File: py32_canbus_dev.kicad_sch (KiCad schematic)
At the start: 42 parts, among them J2 Conn_01x18, J3 Conn_01x18, J4 CAN1, J5 USB_B_Micro, SW2 Reset, U1 uA7805, U2 PY32F030K1xT, U3 MCP2518FD-E/QBB, U4 MCP2562FD-E/MF, U5 FT230XQ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

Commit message: Completed schematic and pcb check
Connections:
- net GND: no longer J2.8 (Pin_8), J2.9 (Pin_9)
- net PA11: now also J2.15 (Pin_15); no longer J2.17 (Pin_17)
- net PA12: now also J2.14 (Pin_14); no longer J2.16 (Pin_16)
- net PA15: now also J2.13 (Pin_13); no longer J2.15 (Pin_15)
- net PB3: now also J2.12 (Pin_12); no longer J2.14 (Pin_14)
- net PB4: now also J2.11 (Pin_11); no longer J2.13 (Pin_13)
- net PB5: now also J2.10 (Pin_10); no longer J2.12 (Pin_12)
- net USB_RX: now also J2.8 (Pin_8); no longer J2.10 (Pin_10)
- net USB_TX: now also J2.9 (Pin_9); no longer J2.11 (Pin_11)
- net OSC32IN renamed PA10
- net PA10: now also J2.16 (Pin_16)
- net OSC32OUT renamed PA9
- net PA9: now also J2.17 (Pin_17)
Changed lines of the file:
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@@
 	)
 	(junction
-		(at 232.41 44.45)
-		(diameter 0)
-		(color 0 0 0 0)
-	)
-	(junction
 		(at 130.81 34.29)
 		(diameter 0)
@@
 	)
 	(junction
-		(at 232.41 46.99)
-		(diameter 0)
-		(color 0 0 0 0)
-	)
-	(junction
 		(at 238.76 147.32)
 		(diameter 0)
@@
 	(wire
 		(pts
-			(xy 232.41 46.99) (xy 232.41 82.55)
-		)
-		(stroke
-			(width 0)
-			(type default)
-		)
-	)
-	(wire
-		(pts
 			(xy 52.07 135.89) (xy 52.07 139.7)
 		)
@@
 	(wire
 		(pts
-			(xy 232.41 41.91) (xy 232.41 44.45)
+			(xy 232.41 41.91) (xy 232.41 82.55)
 		)
 		(stroke
@@
 	(wire
 		(pts
-			(xy 232.41 46.99) (xy 245.11 46.99)
-		)
-		(stroke
-			(width 0)
-			(type default)
-		)
-	)
-	(wire
-		(pts
 			(xy 139.7 175.26) (xy 139.7 177.8)
 		)
@@
 	(wire
 		(pts
-			(xy 232.41 44.45) (xy 232.41 46.99)
-		)
-		(stroke
-			(width 0)
-			(type default)
-		)
-	)
-	(wire
-		(pts
-			(xy 232.41 44.45) (xy 245.11 44.45)
-		)
-		(stroke
-			(width 0)
-			(type default)
-		)
-	)
-	(wire
-		(pts
 			(xy 27.94 59.69) (xy 27.94 49.53)
 		)
@@
 	(global_label "PA15"
 		(shape bidirectional)
-		(at 245.11 62.23 180)
+		(at 245.11 57.15 180)
+		(fields_autoplaced yes)
+		(effects
+			(font
+				(size 1.27 1.27)
+			)
+			(justify right)
+		)
+		(property "Intersheetrefs" "${INTERSHEET_REFS}"
+			(at 237.9193 57.2294 0)
+			(effects
+				(font
+					(size 1.27 1.27)
+				)
+				(justify right)
+				(hide yes)
+			)
+		)
+	)
+	(global_label "PA10"
+		(shape bidirectional)
+		(at 245.11 64.77 180)
 		(fields_autoplaced yes)
 		(effects
@@
 		)
 		(property "Intersheetrefs" "${INTERSHEET_REFS}"
-			(at 237.9193 62.3094 0)
+			(at 236.2359 64.77 0)
 			(effects
 				(font
@@
 		)
 	)
-	(global_label "OSC32OUT"
-		(shape output)
+	(global_label "PA9"
+		(shape bidirectional)
 		(at 162.56 105.41 0)
 		(fields_autoplaced yes)
@@
 		)
 		(property "Intersheetrefs" "${INTERSHEET_REFS}"
-			(at 174.8307 105.4894 0)
+			(at 170.2246 105.41 0)
 			(effects
 				(font
@@
 		)
 	)
-	(global_label "OSC32IN"
-		(shape input)
+	(global_label "PA10"
+		(shape bidirectional)
 		(at 162.56 102.87 0)
 		(fields_autoplaced yes)
@@
 		)
 		(property "Intersheetrefs" "${INTERSHEET_REFS}"
-			(at 173.1374 102.9494 0)
+			(at 171.4341 102.87 0)
 			(effects
 				(font
@@
 		)
 	)
+	(global_label "PA9"
+		(shape bidirectional)
+		(at 245.11 67.31 180)
+		(fields_autoplaced yes)
+		(effects
+			(font
+				(size 1.27 1.27)
+			)
+			(justify right)
+		)
+		(property "Intersheetrefs" "${INTERSHEET_REFS}"
+			(at 237.4454 67.31 0)
+			(effects
+				(font
+					(size 1.27 1.27)
+				)
+				(justify right)
+				(hide yes)
+			)
+		)
+	)
 	(global_label "SPI1-NSS"
 		(shape input)
@@
 	(global_label "PB4"
 		(shape bidirectional)
-		(at 245.11 57.15 180)
+		(at 245.11 52.07 180)
 		(fields_autoplaced yes)
 		(effects
@@
 		)
 		(property "Intersheetrefs" "${INTERSHEET_REFS}"
-			(at 238.9474 57.0706 0)
+			(at 238.9474 51.9906 0)
 			(effects
 				(font
@@
 	(global_label "PB3"
 		(shape bidirectional)
-		(at 245.11 59.69 180)
+		(at 245.11 54.61 180)
 		(fields_autoplaced yes)
 		(effects
@@
 		)
 		(property "Intersheetrefs" "${INTERSHEET_REFS}"
-			(at 238.9474 59.6106 0)
+			(at 238.9474 54.5306 0)
 			(effects
 				(font
@@
 	(global_label "USB_RX"
 		(shape input)
-		(at 245.11 49.53 180)
+		(at 245.11 44.45 180)
 		(fields_autoplaced yes)
 		(effects
@@
 		)
 		(property "Intersheetrefs" "${INTERSHEET_REFS}"
-			(at 234.8677 49.53 0)
+			(at 234.8677 44.45 0)
 			(effects
 				(font
@@
 	(global_label "USB_TX"
 		(shape output)
-		(at 245.11 52.07 180)
+		(at 245.11 46.99 180)
 		(fields_autoplaced yes)
 		(effects
@@
 		)
 		(property "Intersheetrefs" "${INTERSHEET_REFS}"
-			(at 235.1701 52.07 0)
+			(at 235.1701 46.99 0)
 			(effects
 				(font
@@
 	(global_label "PB5"
 		(shape bidirectional)
-		(at 245.11 54.61 180)
+		(at 245.11 49.53 180)
 		(fields_autoplaced yes)
 		(effects
@@
 		)
 		(property "Intersheetrefs" "${INTERSHEET_REFS}"
-			(at 238.9474 54.5306 0)
+			(at 238.9474 49.4506 0)
 			(effects
 				(font
@@
 	(global_label "PA12"
 		(shape bidirectional)
-		(at 245.11 64.77 180)
+		(at 245.11 59.69 180)
 		(fields_autoplaced yes)
 		(effects
@@
 		)
 		(property "Intersheetrefs" "${INTERSHEET_REFS}"
-			(at 237.9193 64.6906 0)
+			(at 237.9193 59.6106 0)
 			(effects
 				(font
@@
 	(global_label "PA11"
 		(shape bidirectional)
-		(at 245.11 67.31 180)
+		(at 245.11 62.23 180)
 		(fields_autoplaced yes)
 		(effects
@@
 		)
 		(property "Intersheetrefs" "${INTERSHEET_REFS}"
-			(at 237.9193 67.2306 0)
+			(at 237.9193 62.1506 0)
 			(effects
 				(font
@@
 			(at 238.76 135.89 0)
 			(effects
-				(font
-					(size 1.27 1.27)
-				)
-				(hide yes)
-			)
-		)
-		(property "Field5" ""
-			(at 238.76 135.89 0)
-			(effects

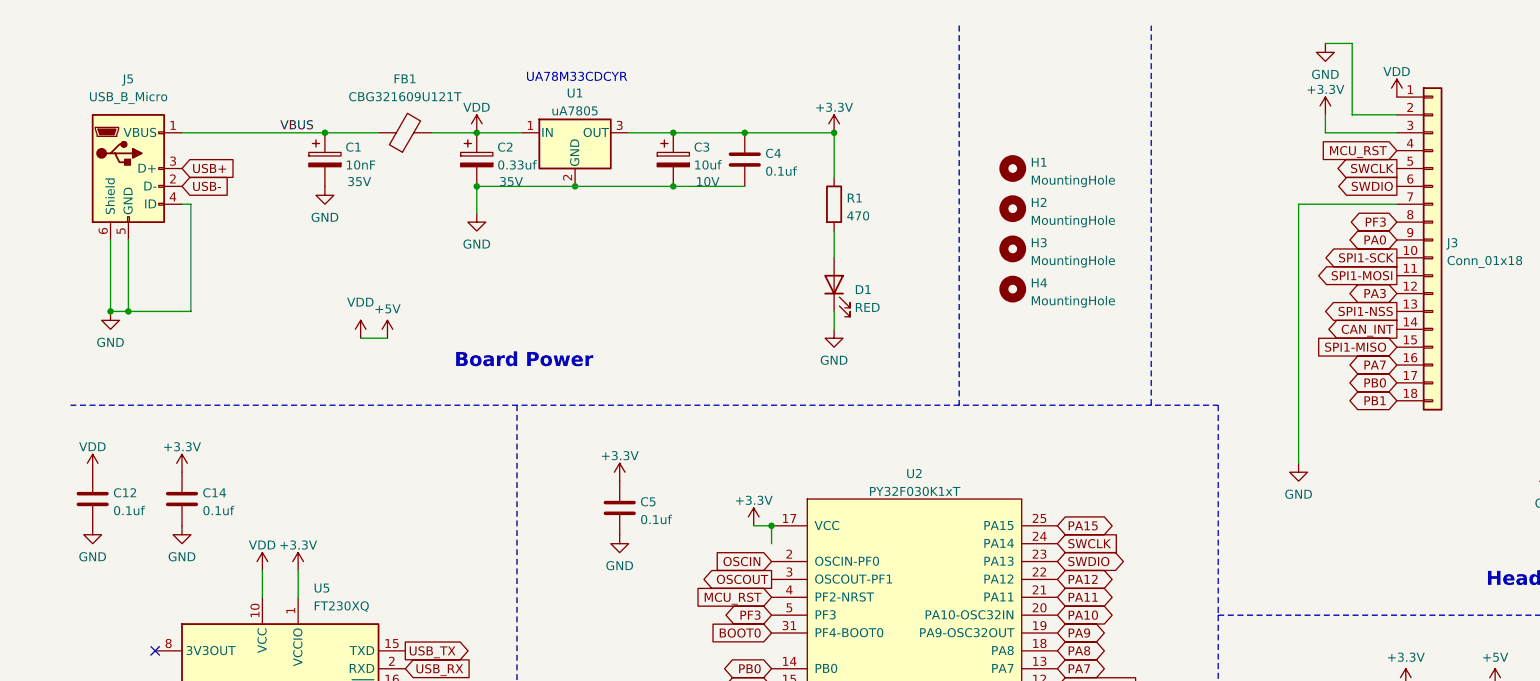
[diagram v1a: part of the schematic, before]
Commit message: Removed VDD
Adding LCSC part numbers to BOM
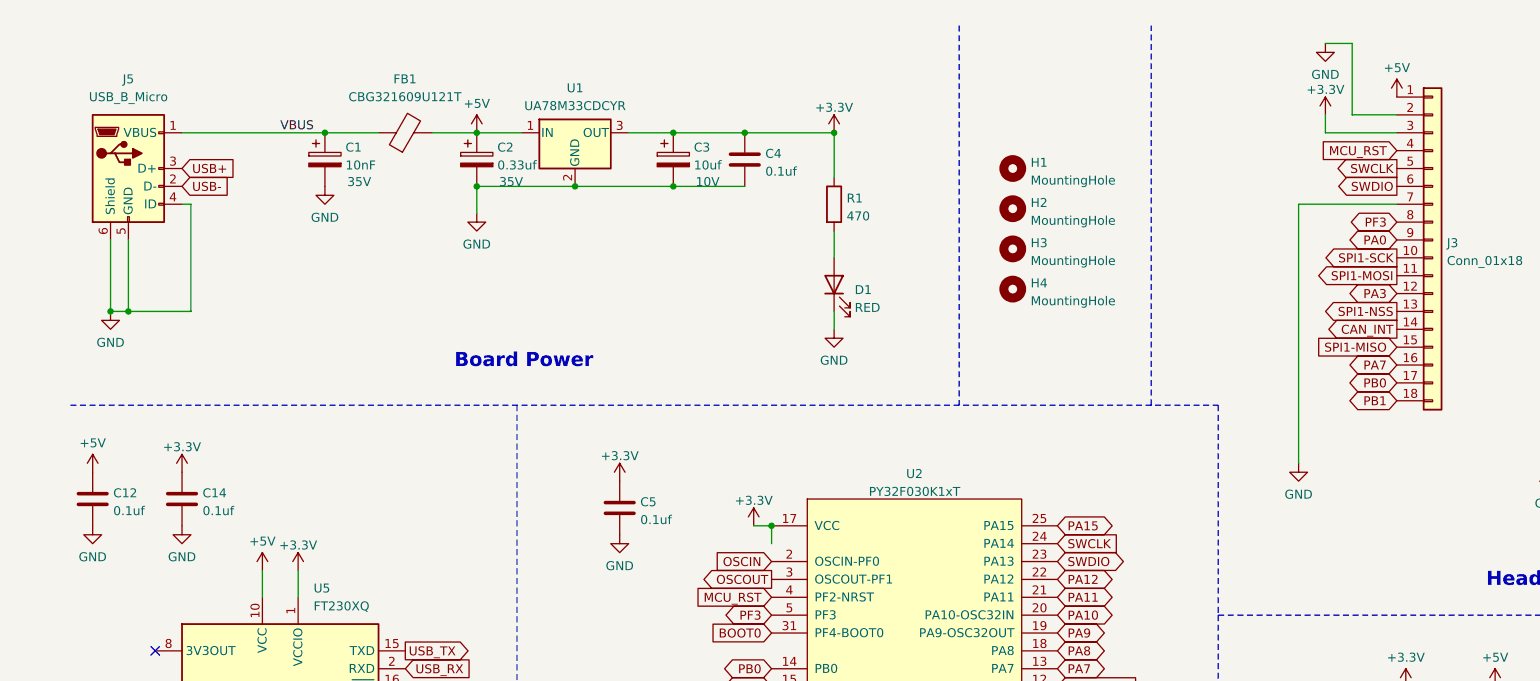
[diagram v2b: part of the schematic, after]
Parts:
- U1: value uA7805 -> UA78M33CDCYR
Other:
- note removed: "UA78M33CDCYR"

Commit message: Fixed usb tx and rx
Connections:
- net USB_RX: now also U2.29 (PB6); no longer U2.30 (PB7)
- net USB_TX: now also U2.30 (PB7); no longer U2.29 (PB6)
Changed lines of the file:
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@@
-	)
-	(junction
-		(at 121.92 90.17)
-		(diameter 0)
-		(color 0 0 0 0)
 	)
 	(junction
@@
 	(wire
 		(pts
-			(xy 121.92 90.17) (xy 121.92 92.71)
-		)
-		(stroke
-			(width 0)
-			(type default)
-		)
-	)
-	(wire
-		(pts
 			(xy 245.11 41.91) (xy 232.41 41.91)
 		)
@@
 	(global_label "USB_RX"
 		(shape input)
-		(at 121.92 125.73 180)
+		(at 121.92 123.19 180)
 		(fields_autoplaced yes)
 		(effects
@@
 		)
 		(property "Intersheetrefs" "${INTERSHEET_REFS}"
-			(at 111.6777 125.73 0)
+			(at 111.6777 123.19 0)
 			(effects
 				(font
@@
 	(global_label "USB_TX"
 		(shape output)
-		(at 121.92 123.19 180)
+		(at 121.92 125.73 180)
 		(fields_autoplaced yes)
 		(effects
@@
 		)
 		(property "Intersheetrefs" "${INTERSHEET_REFS}"
-			(at 111.9801 123.19 0)
-			(effects
-				(font
+			(at 111.9801 125.73 0)
+			(effects
+				(font

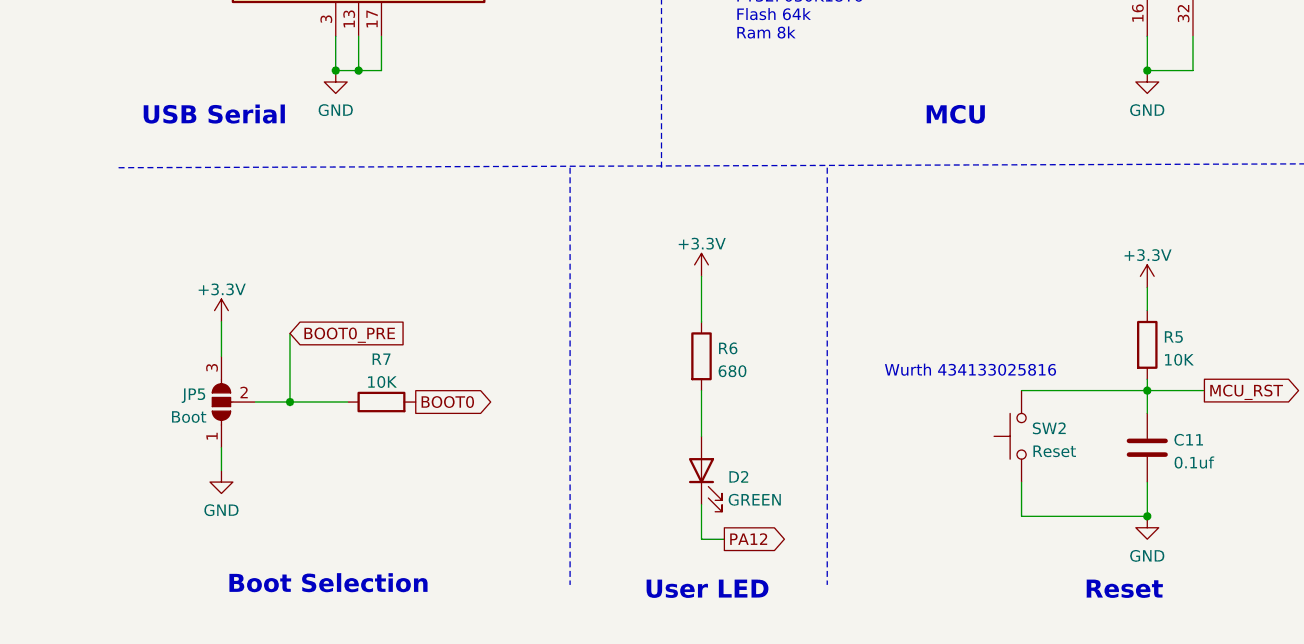
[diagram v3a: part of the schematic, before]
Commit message: Upped hole diameter, added 2 leds
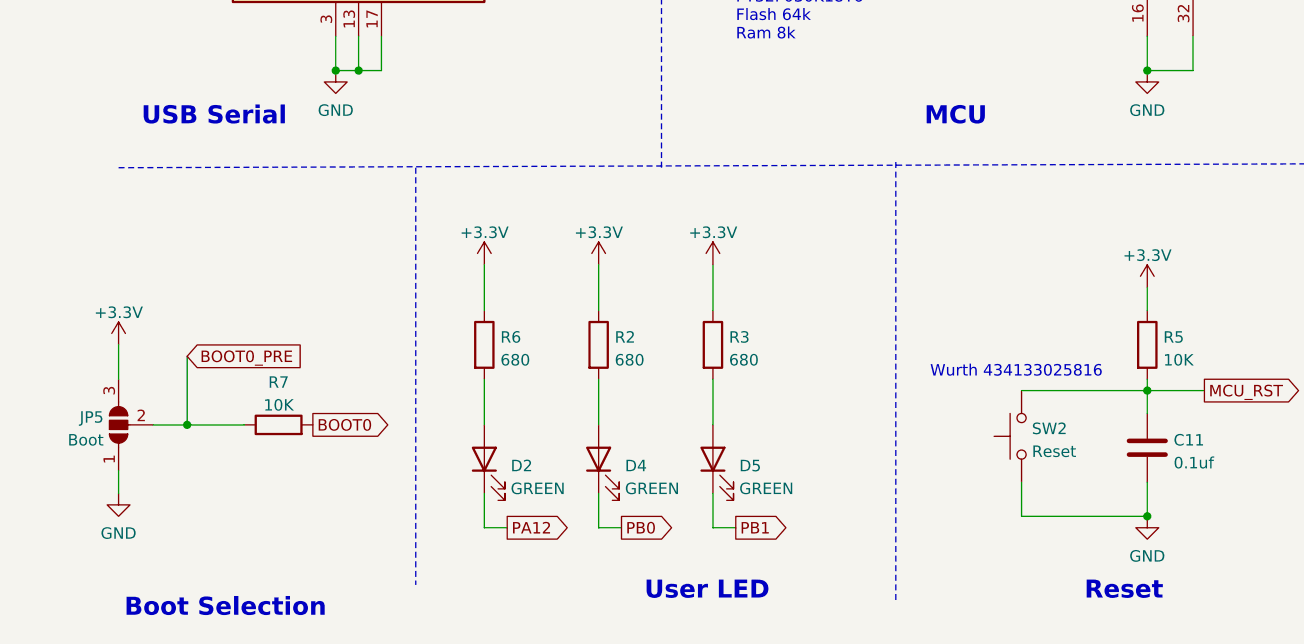
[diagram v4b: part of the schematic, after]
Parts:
- added D4, D5: GREEN, Diode_SMD:D_0603_1608Metric, symbol Device:LED
- added R2, R3: 680, Resistor_SMD:R_0603_1608Metric, symbol Device:R
- H1, H2, H3, H4: footprint MountingHole:MountingHole_2.5mm_Pad -> MountingHole:MountingHole_3.2mm_M3
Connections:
- net +3.3V: now also R2.1, R3.1
- net PB0: now also D4.1 (K)
- net PB1: now also D5.1 (K)
- new net: D5.2 (A), R3.2
- new net: D4.2 (A), R2.2
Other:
- moved on the sheet: D2, JP5, R6, R7
